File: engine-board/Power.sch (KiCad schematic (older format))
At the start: 17 parts, among them J401 USB/SER/CHRGR, J402 Power Rail, J403 Engine Current Sensor, J404 RAW_BATT-, J406 3V Current Sensor, J407 5V Current Sensor, J408 RAW_BATT+, J409 RAW_BATT-, J410 RAW_BATT+, J411 RAW_BATT-, J412 RAW_BATT+, J413 Batt_Therm, J414 Batt Sense, SW401 POWER, U401 Pololu_2814, U402 R-78B3.3-2.0, U403 R-78B5.0-2.0

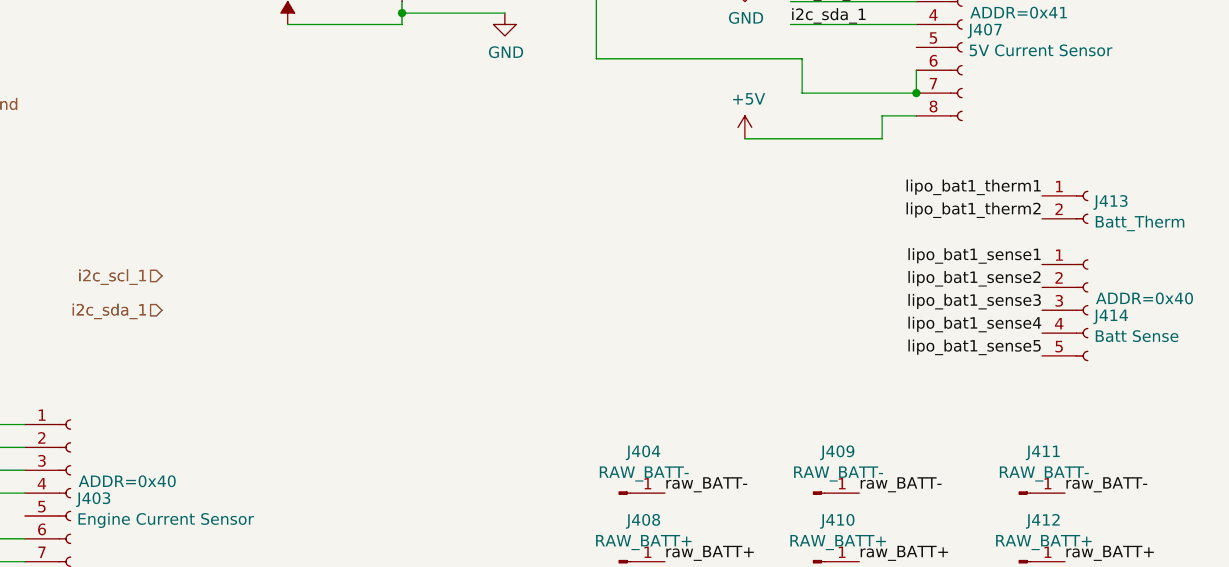
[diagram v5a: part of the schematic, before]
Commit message: board smaller
PCB V0.1 Errata:

- [QUESTION: - it looks like 12 on website] polulu 2814 has 16 pin footprint instead of 12...  AAACK!!!
- 5v and 3.3v traces could be wider
- [FIXED] fail: going into the power schematic scl + sda are swapped...
- [FIXED - moved to miniofit] pump controller silkscreen is wrong
- [FIXED] NOTE: just switch ALL to the minifit??
- [FIXED - will be on top, but not needed now] ADD: Ethernet connection from the teensy to the host computer board.
- [FIXED - going to use Qwiic) 9 Axis Mopak: wrong footprint - holes too small, spacing seems good, create outline as it bumps into feather header
- [FIXED] RV1805:  power + GND swapped... and I can’t seem to find them.
- [FIXED] 2 pressure sensors, the same i2c address... rerouted to 2nd i2c port on teensy
- [NOT NEEDED - adding display] Add RGB LED... it will be helpful for debugging.
- [FIXED - kindof - moved to micro-fit, might need to wire this directly to bulkhead] Turbine ferrules for power are 12 gauge - need bigger screw terminals if that is the connection method
- [FIXED] Feather footprint - lookup exactly what feather boards need for support..
- [FIXED] pump_motor_pwm is not connected to the TEENSY!!  blerg.  (jumper to pin 13 of feather for now)
- [FIXED - added FET] Maxon 70/30 POWER?  Think about power FET or ‘sleep’ to turn it off.
- [FIXED - added to bulkhead connector] Teensy 4.1 Program + ON/OFF pins - research how to extend these
- [TODO] remove VL6180 range sensor
- [LATER - will add to cost.. possibly remove?] put battery on back side
- add silkscreen for polulu
- [FIXED] Reorganize connectors:
    - Pump motor connectors go on end - attached in closing
    - bulkhead connectors go on side as they will always be attached
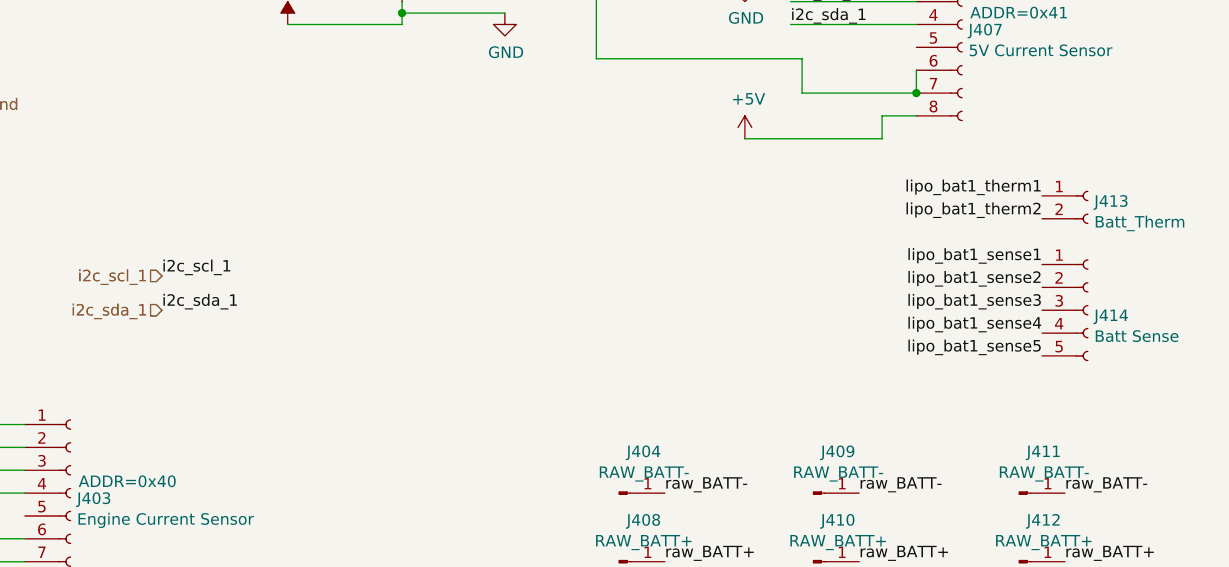
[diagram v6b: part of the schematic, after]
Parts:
- J401: MATE_MPM 0430251608 -> (none); MATE_MPN (none) -> 0430251608
- J402: Link https://www.digikey.com/en/products/detail/samtec-inc/SSQ-1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 -> https://www.digikey.com/en/products/detail/samtec-inc/TSW-1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; MPN SSQ-108-01-G-S -> TSW-108-05-G-S; Price 1.68 -> 0.96
- J403, J406, J407: Link https://www.digikey.com/en/products/detail/samtec-inc/SSQ-106-01-G-S/1110613 -> https://www.digikey.com/en/products/detail/samtec-inc/SSQ-108-01-G-S/1110611; MATE_Link (none) -> https://www.digikey.com/en/products/detail/molex/0901210128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; MATE_MPN (none) -> 0901210128; MATE_Price (none) -> 1.16; Manufacturer (none) -> Adafruit
- J414: I2C_ADDR ADDR=0x40 -> (none); Link https://www.digikey.com/en/products/detail/samtec-inc/SSQ-1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 -> (none); Link2 https://www.adafruit.com/product/4226 -> (none); MANUFACTURER Samtec Inc. -> (none); MPN SSQ-108-01-G-S -> (none); Price 1.35 -> (none); Price2 9.95 -> (none)
- SW401: Link (none) -> https://www.adafruit.com/product/805; MPN (none) -> 805; Manufacturer (none) -> Adafruit
- U401: footprint Module:Pololu_Breakout-16_15.2x20.3mm -> Sensor_Current:Polulu_2814; Link https://www.pololu.com/product/2814 -> https://www.digikey.com/en/products/detail/samtec-inc/SSQ-1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; Link2 (none) -> https://www.pololu.com/product/2814; MATE_Link (none) -> https://www.digikey.com/en/products/detail/samtec-inc/SSQ-1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; MATE_MPN (none) -> SSQ-104-01-G-S; MATE_Price (none) -> 1.35; MPM 2814 -> (none); MPN (none) -> SSQ-106-01-G-S; MPN2 (none) -> 2814; Manufacturer (none) -> Polulu; Price 4.75 -> 1.35; Price2 (none) -> 4.75
- U402: MPM R-78B3.3-2.0 -> (none); MPN (none) -> R-78B3.3-2.0
- U403: MPM R-78B5.0-2.0 -> (none); MPN (none) -> R-78B5.0-2.0
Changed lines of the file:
@@
 F 6 "430451623" H 1250 2050 50  0001 C CNN "MPN"
 F 7 "6.91" H 1250 2050 50  0001 C CNN "Price"
-F 8 "0430251608" H 1250 2050 50  0001 C CNN "MATE_MPM"
+F 8 "" H 1250 2050 50  0001 C CNN "MATE_MPM"
 F 9 "1.61" H 1250 2050 50  0001 C CNN "MATE_Price"
 F 10 "https://www.digikey.com/en/products/detail/molex/0430251608/3310170" H 1250 2050 50  0001 C CNN "MATE_Link"
 F 11 "" H 1250 2050 50  0001 C CNN "Field11"
+F 12 "0430251608" H 1250 2050 50  0001 C CNN "MATE_MPN"
 	1    1250 2050
 	-1   0    0    -1
@@
 F 3 "https://www.recom-power.com/pdf/Innoline/R-78Bxx-2.0.pdf" H 5450 900 50  0001 C CNN
 F 4 "https://www.digikey.com/en/products/detail/recom-power/R-78B3-3-2-0/6677082" H 5450 900 50  0001 C CNN "Link"
-F 5 "R-78B3.3-2.0" H 5450 900 50  0001 C CNN "MPM"
+F 5 "" H 5450 900 50  0001 C CNN "MPM"
 F 6 "11.35" H 5450 900 50  0001 C CNN "Price"
+F 7 "R-78B3.3-2.0" H 5450 900 50  0001 C CNN "MPN"
 	1    5450 900
 	1    0    0    -1
@@
 F 3 "https://www.recom-power.com/pdf/Innoline/R-78Bxx-2.0.pdf" H 5500 2150 50  0001 C CNN
 F 4 "https://www.digikey.com/en/products/detail/recom-power/R-78B5-0-2-0/6677084" H 5500 2150 50  0001 C CNN "Link"
-F 5 "R-78B5.0-2.0" H 5500 2150 50  0001 C CNN "MPM"
+F 5 "" H 5500 2150 50  0001 C CNN "MPM"
 F 6 "11.35" H 5500 2150 50  0001 C CNN "Price"
+F 7 "R-78B5.0-2.0" H 5500 2150 50  0001 C CNN "MPN"
 	1    5500 2150
 	1    0    0    -1
@@
 F 0 "U401" H 4400 7365 50  0000 C CNN
 F 1 "Pololu_2814" H 4400 7274 50  0000 C CNN
-F 2 "Module:Pololu_Breakout-16_15.2x20.3mm" H 4350 7250 50  0001 C CNN
+F 2 "Sensor_Current:Polulu_2814" H 4350 7250 50  0001 C CNN
 F 3 "https://www.pololu.com/product/2814" H 4350 7250 50  0001 C CNN
-F 4 "https://www.pololu.com/product/2814" H 4300 6400 50  0001 C CNN "Link"
-F 5 "2814" H 4300 6400 50  0001 C CNN "MPM"
-F 6 "4.75" H 4300 6400 50  0001 C CNN "Price"
+F 4 "https://www.digikey.com/en/products/detail/samtec-inc/SSQ-106-01-G-S/1110613" H 4300 6400 50  0001 C CNN "Link"
+F 5 "" H 4300 6400 50  0001 C CNN "MPM"
+F 6 "1.35" H 4300 6400 50  0001 C CNN "Price"
+F 7 "SSQ-106-01-G-S" H 4300 6400 50  0001 C CNN "MPN"
+F 8 "https://www.pololu.com/product/2814" H 4300 6400 50  0001 C CNN "Link2"
+F 9 "https://www.digikey.com/en/products/detail/samtec-inc/SSQ-106-01-G-S/1110613" H 4300 6400 50  0001 C CNN "MATE_Link"
+F 10 "SSQ-104-01-G-S" H 4300 6400 50  0001 C CNN "MATE_MPN"
+F 11 "1.35" H 4300 6400 50  0001 C CNN "MATE_Price"
+F 12 "2814" H 4300 6400 50  0001 C CNN "MPN2"
+F 13 "Polulu" H 4300 6400 50  0001 C CNN "Manufacturer"
+F 14 "4.75" H 4300 6400 50  0001 C CNN "Price2"
 	1    4300 6400
 	1    0    0    -1
@@
 F 2 "Connector_PinSocket_2.54mm:PinSocket_1x08_P2.54mm_Vertical" H 2350 4950 50  0001 C CNN
 F 3 "~" H 2350 4950 50  0001 C CNN
-F 4 "https://www.digikey.com/en/products/detail/samtec-inc/SSQ-108-01-G-S/1110611" H 2350 4950 50  0001 C CNN "Link"
+F 4 "https://www.digikey.com/en/products/detail/samtec-inc/TSW-108-05-G-S/1100513" H 2350 4950 50  0001 C CNN "Link"
 F 5 "Samtec Inc." H 2350 4950 50  0001 C CNN "MANUFACTURER"
-F 6 "SSQ-108-01-G-S" H 2350 4950 50  0001 C CNN "MPN"
-F 7 "1.68" H 2350 4950 50  0001 C CNN "Price"
+F 6 "TSW-108-05-G-S" H 2350 4950 50  0001 C CNN "MPN"
+F 7 "0.96" H 2350 4950 50  0001 C CNN "Price"
 	1    2350 4950
 	1    0    0    -1
@@
 F 2 "Connector_PinSocket_2.54mm:PinSocket_1x08_P2.54mm_Vertical" H 4050 4600 50  0001 C CNN
 F 3 "~" H 4050 4600 50  0001 C CNN
-F 4 "https://www.digikey.com/en/products/detail/samtec-inc/SSQ-106-01-G-S/1110613" H 4050 4600 50  0001 C CNN "Link"
+F 4 "https://www.digikey.com/en/products/detail/samtec-inc/SSQ-108-01-G-S/1110611" H 4050 4600 50  0001 C CNN "Link"
 F 5 "Samtec Inc." H 4050 4600 50  0001 C CNN "MANUFACTURER"
 F 6 "SSQ-108-01-G-S" H 4050 4600 50  0001 C CNN "MPN"
@@
 F 9 "https://www.adafruit.com/product/4226" H 4050 4600 50  0001 C CNN "Link2"
 F 10 "ADDR=0x40" H 4300 4650 50  0000 C CNN "I2C_ADDR"
+F 11 "https://www.digikey.com/en/products/detail/molex/0901210128/760817?s=N4IgTCBcDaIJwAYCMYnLADhAXQL5A" H 4050 4600 50  0001 C CNN "MATE_Link"
+F 12 "0901210128" H 4050 4600 50  0001 C CNN "MATE_MPN"
+F 13 "1.16" H 4050 4600 50  0001 C CNN "MATE_Price"
+F 14 "Adafruit" H 4050 4600 50  0001 C CNN "Manufacturer"
 	1    4050 4600
 	1    0    0    -1
@@
 F 2 "Connector_PinSocket_2.54mm:PinSocket_1x08_P2.54mm_Vertical" H 7950 2550 50  0001 C CNN
 F 3 "~" H 7950 2550 50  0001 C CNN
-F 4 "https://www.digikey.com/en/products/detail/samtec-inc/SSQ-106-01-G-S/1110613" H 7950 2550 50  0001 C CNN "Link"
+F 4 "https://www.digikey.com/en/products/detail/samtec-inc/SSQ-108-01-G-S/1110611" H 7950 2550 50  0001 C CNN "Link"
 F 5 "Samtec Inc." H 7950 2550 50  0001 C CNN "MANUFACTURER"
 F 6 "SSQ-108-01-G-S" H 7950 2550 50  0001 C CNN "MPN"
@@
 F 9 "https://www.adafruit.com/product/4226" H 7950 2550 50  0001 C CNN "Link2"
 F 10 "ADDR=0x41" H 8200 2600 50  0000 C CNN "I2C_ADDR"
+F 11 "https://www.digikey.com/en/products/detail/molex/0901210128/760817?s=N4IgTCBcDaIJwAYCMYnLADhAXQL5A" H 7950 2550 50  0001 C CNN "MATE_Link"
+F 12 "0901210128" H 7950 2550 50  0001 C CNN "MATE_MPN"
+F 13 "1.16" H 7950 2550 50  0001 C CNN "MATE_Price"
+F 14 "Adafruit" H 7950 2550 50  0001 C CNN "Manufacturer"
 	1    7950 2550
 	1    0    0    -1
@@
 F 2 "Connector_PinSocket_2.54mm:PinSocket_1x08_P2.54mm_Vertical" H 7950 1250 50  0001 C CNN
 F 3 "~" H 7950 1250 50  0001 C CNN
-F 4 "https://www.digikey.com/en/products/detail/samtec-inc/SSQ-106-01-G-S/1110613" H 7950 1250 50  0001 C CNN "Link"
+F 4 "https://www.digikey.com/en/products/detail/samtec-inc/SSQ-108-01-G-S/1110611" H 7950 1250 50  0001 C CNN "Link"
 F 5 "Samtec Inc." H 7950 1250 50  0001 C CNN "MANUFACTURER"
 F 6 "SSQ-108-01-G-S" H 7950 1250 50  0001 C CNN "MPN"
@@
 F 9 "https://www.adafruit.com/product/4226" H 7950 1250 50  0001 C CNN "Link2"
 F 10 "ADDR=0x44" H 8200 1300 50  0000 C CNN "I2C_ADDR"
+F 11 "https://www.digikey.com/en/products/detail/molex/0901210128/760817?s=N4IgTCBcDaIJwAYCMYnLADhAXQL5A" H 7950 1250 50  0001 C CNN "MATE_Link"
+F 12 "0901210128" H 7950 1250 50  0001 C CNN "MATE_MPN"
+F 13 "1.16" H 7950 1250 50  0001 C CNN "MATE_Price"
+F 14 "Adafruit" H 7950 1250 50  0001 C CNN "Manufacturer"
 	1    7950 1250
 	1    0    0    -1
@@
 F 3 "https://www.adafruit.com/product/805" H 2450 6802 60  0001 C CNN
 F 4 "0.95" H 2450 6600 50  0001 C CNN "Price"
+F 5 "https://www.adafruit.com/product/805" H 2450 6600 50  0001 C CNN "Link"
+F 6 "805" H 2450 6600 50  0001 C CNN "MPN"
+F 7 "Adafruit" H 2450 6600 50  0001 C CNN "Manufacturer"
 	1    2450 6600
 	1    0    0    -1
@@
 F 2 "Connector_Wire:SolderWire-0.5sqmm_1x05_P4.6mm_D0.9mm_OD2.1mm_Relief" H 8500 3800 50  0001 C CNN
 F 3 "~" H 8500 3800 50  0001 C CNN
-F 4 "https://www.digikey.com/en/products/detail/samtec-inc/SSQ-106-01-G-S/1110613" H 8500 3800 50  0001 C CNN "Link"
-F 5 "Samtec Inc." H 8500 3800 50  0001 C CNN "MANUFACTURER"
-F 6 "SSQ-108-01-G-S" H 8500 3800 50  0001 C CNN "MPN"
-F 7 "1.35" H 8500 3800 50  0001 C CNN "Price"
-F 8 "9.95" H 8500 3800 50  0001 C CNN "Price2"
-F 9 "https://www.adafruit.com/product/4226" H 8500 3800 50  0001 C CNN "Link2"
-F 10 "ADDR=0x40" H 8750 3850 50  0000 C CNN "I2C_ADDR"
+F 4 "" H 8500 3800 50  0001 C CNN "Link"
+F 5 "" H 8500 3800 50  0001 C CNN "MANUFACTURER"
+F 6 "" H 8500 3800 50  0001 C CNN "MPN"
+F 7 "" H 8500 3800 50  0001 C CNN "Price"
+F 8 "" H 8500 3800 50  0001 C CNN "Price2"
+F 9 "" H 8500 3800 50  0001 C CNN "Link2"
+F 10 "" H 8750 3850 50  0000 C CNN "I2C_ADDR"
+F 11 "" H 8500 3800 50  0001 C CNN "MATE_Link"
+F 12 "" H 8500 3800 50  0001 C CNN "MATE_MPN"
+F 13 "" H 8500 3800 50  0001 C CNN "MATE_Price"
+F 14 "" H 8500 3800 50  0001 C CNN "Manufacturer"
 	1    8500 3800
 	1    0    0    -1
@@
 	1    0    0    -1
 $EndComp
+Text Label 4450 3650 0    50   ~ 0
+i2c_scl_1
+Text Label 4450 3800 0    50   ~ 0
+i2c_sda_1
 $EndSCHEMATC
